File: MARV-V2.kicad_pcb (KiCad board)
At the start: 4 copper layers, 50.7 x 45.5 mm, 107 parts, among them J10 DBG pads (SWCLK SWDIO GND), J11 microSD, Molex 47219-2001 loc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, J3 ESC pads (CURR TX M4 M3 M2 M1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, J4 USB_C_PROGRAM_POWER, J6 IO array signal column (inner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, J7 IO array power column (5V / 3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, J8 IO array GND column (board ed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, Q1 AO3401A, SW1 RESET (RUN to GND), SW2 BOOTSEL (via R24), U12 TPS7A2033PDBVR, U20 RP2354B, U21 ICM-45686 6-axis IMU, U22 BMP581 barometer, U23 ADXL375 high-g accelerometer, U24 DNP: W25Q32JVSNIQ, 32 Mbit QS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, U7 AP63203WU-7, Y1 12 MHz TAXM12M4RFBCCT2T, CL 1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

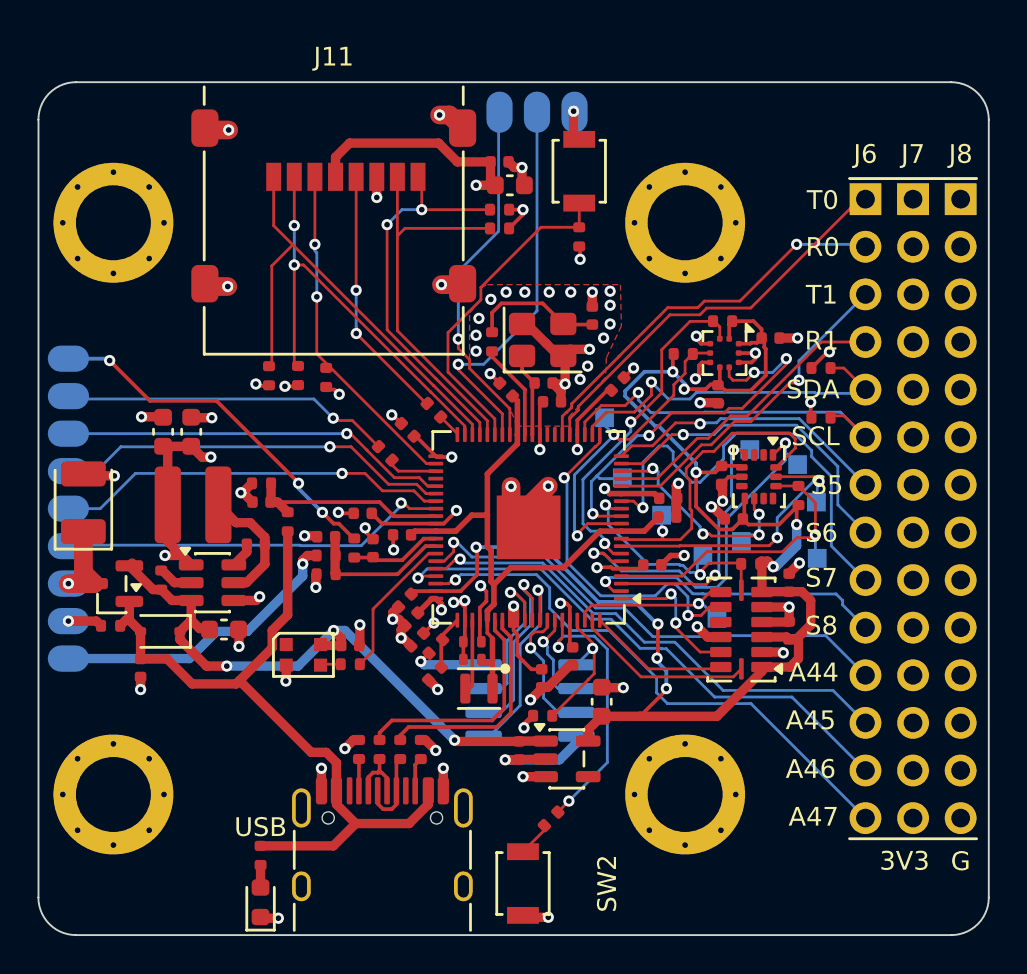
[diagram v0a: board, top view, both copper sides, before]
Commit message: Order-ready: core regulator per RP2350 §6.3.8, SWD header, second DVDD cap, README rewrite
Core regulator (U20 / C39 / C45 / L20):
- C39/C45 lands narrowed to 0.46 mm (0.50 mm gap) so VREG_LX passes between
  the pads as in datasheet Fig. 23; local 0.12 mm clearance rule for those
  two footprints only (inside JLC's 3.5 mil four-layer tier)
- In1 GND cutout under L20 and the LX net (Fig. 24); single-point ground
  return with two adjacent vias; B.Cu GND pour tying the SD-cluster vias
- L20 switched to the polarity-marked Abracon AOTA-B201610S3R3-101-T
  (LCSC C42411119) with a silk orientation dot at pad 2 / DVDD
- C81 added: second 4.7 uF on DVDD at the far edge of the package
- U22 BMP581: traces/vias moved out from under the body, mask window opened

Debug: J10 is now a 1x03 2.54 mm THT header wired SWCLK-GND-SWDIO
(Raspberry Pi Debug Probe order); checker, exporter, BOM sources and DFM
rules updated to match.

DFM: courtyard rules relaxed to JLC's body-to-body equivalents (non-overlap
for chip/SOT/SOIC, 0.5 mm courtyard gap IC-to-IC); all 81 findings cleared
without moving parts. DRC 0 errors, 0 unconnected, 0 parity; ERC 0.

Docs: README rewritten around the board, sensor suite, power architecture,
design decisions (external conversion, Q1/D1 OR, sensor LDO, native SD over
PIO, locking microSD socket, fab tier) and the input-power simulation;
DESIGN_SPEC status text brought current; communication-architecture.md
marked historical. Stale root MARV-V2.drl removed (exports live in build/).

Co-Authored-By: Claude Fable 5.1 <noreply@anthropic.com>
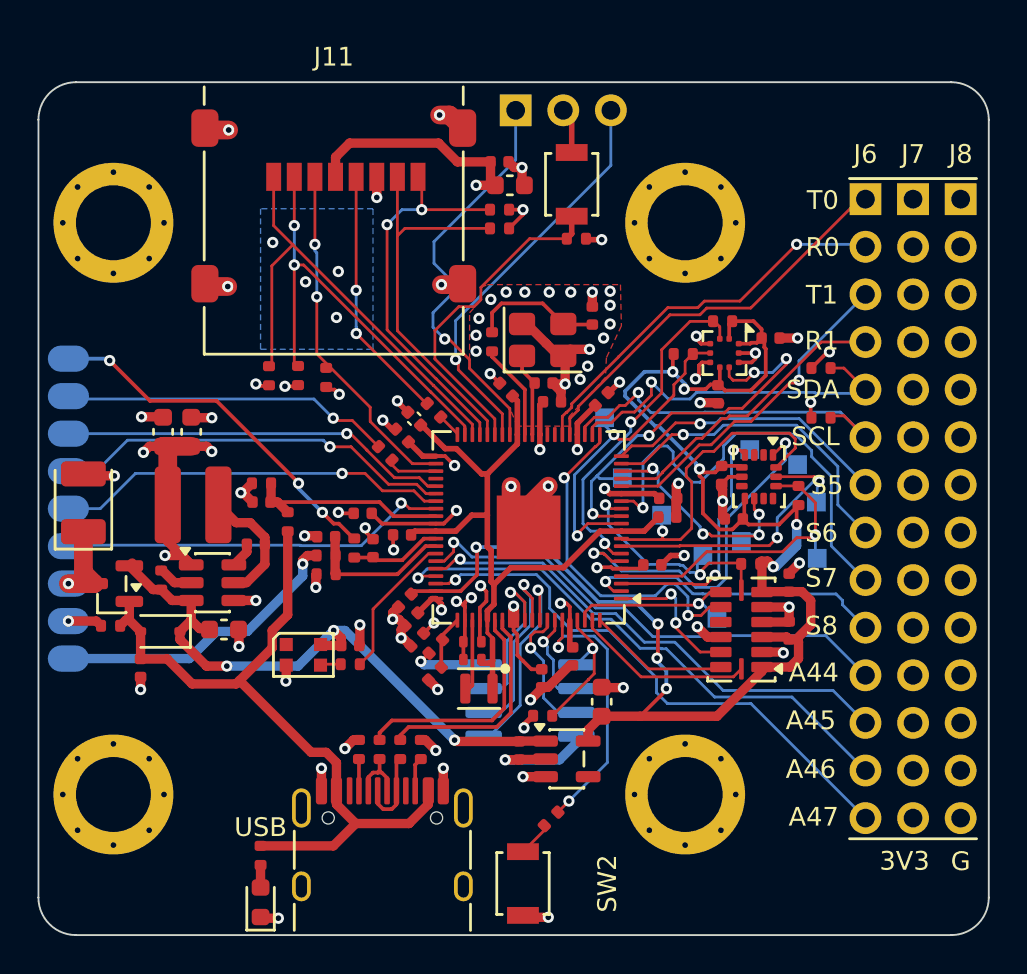
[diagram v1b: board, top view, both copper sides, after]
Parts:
- added C81: 4.7u / 10 V X5R 0402, DVDD second bulk, far edge of U20 (RP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, Capacitor_SMD:C_0402_1005Metric, F.Cu at (94.7, 95.2)
- J10: value DBG pads (SWCLK SWDIO GND) -> SWD header 1x03 2.54 mm (SWCLK GND SWDIO); footprint MARV_Packages:PadRow_1x03_P2.00mm -> Connector_PinHeader_2.54mm:PinHeader_1x03_P2.54mm_Vertical
- moved C32 1.17 mm to (104.7, 94.2)
- moved J10 1.14 mm to (100.1, 78.8), turned to -90 degrees
- moved SW1 0.81 mm to (103.1, 82.7)
- moved C34 0.42 mm to (94.0, 96.1)
- moved R10 0.18 mm to (103.3, 85.6), turned to 180 degrees
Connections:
- J10 pad 2: SWDIO -> GND
- J10 pad 3: GND -> SWDIO
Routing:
- net DVDD: track 32.4 -> 37.0 mm
- net SWCLK: track 19.3 -> 21.7 mm
- net GND: track 88.6 -> 90.5 mm, vias 71 -> 74
- net SWDIO: track 20.7 -> 21.8 mm
- net V3V3_SYS: track 72.0 -> 72.8 mm, vias 24 -> 25
- added copper zone on B.Cu, net GND

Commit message: Top silkscreen: sensor axis marker (G1) and chevron (G2) as board-only footprints
Logo_AxisMarker (6 mm, from images/axis_marker_y_right.svg) and Logo_Chevron
(16 mm, straightened and mirrored from the bitmap trace in images/chevron.svg)
added to MARV_Packages.pretty and placed on F.SilkS. Old axis marker SVG removed.

Co-Authored-By: Claude Fable 5.1 <noreply@anthropic.com>
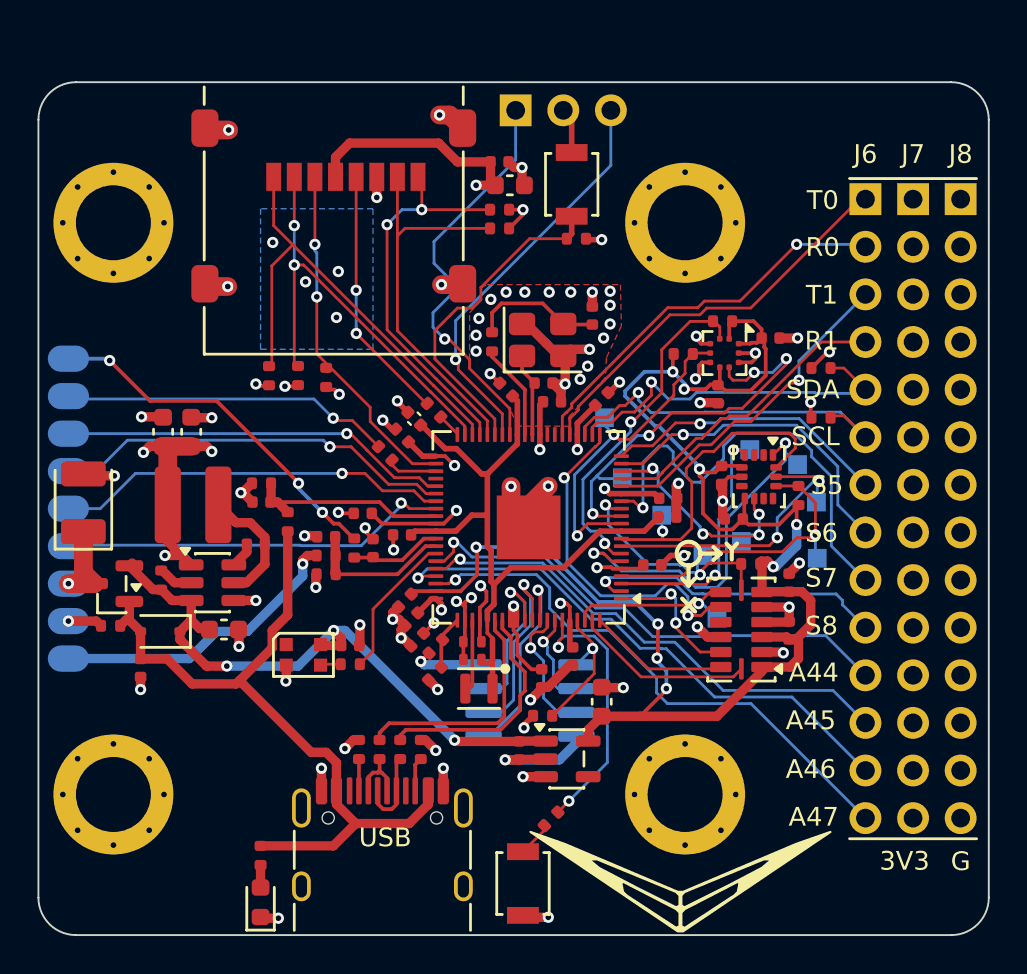
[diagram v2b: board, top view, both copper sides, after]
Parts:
- added G1: Logo_AxisMarker, MARV_Packages:Logo_AxisMarker, F.Cu at (109.7, 103.3)
- added G2: Logo_Chevron, MARV_Packages:Logo_Chevron, F.Cu at (108.9, 119.9)
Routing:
- net USB_DP_RP: track 11.8 -> 12.6 mm
